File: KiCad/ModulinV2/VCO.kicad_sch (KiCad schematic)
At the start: 107 parts, among them IC13 AS3340D, IC14 AS3340D, IC15 TL074HIDR, IC16 TL074HIDR, IC17 TL072HIDR, Q1 MMBFJ201, Q2 MMBFJ201, SW1 SW_SPDT_MSM

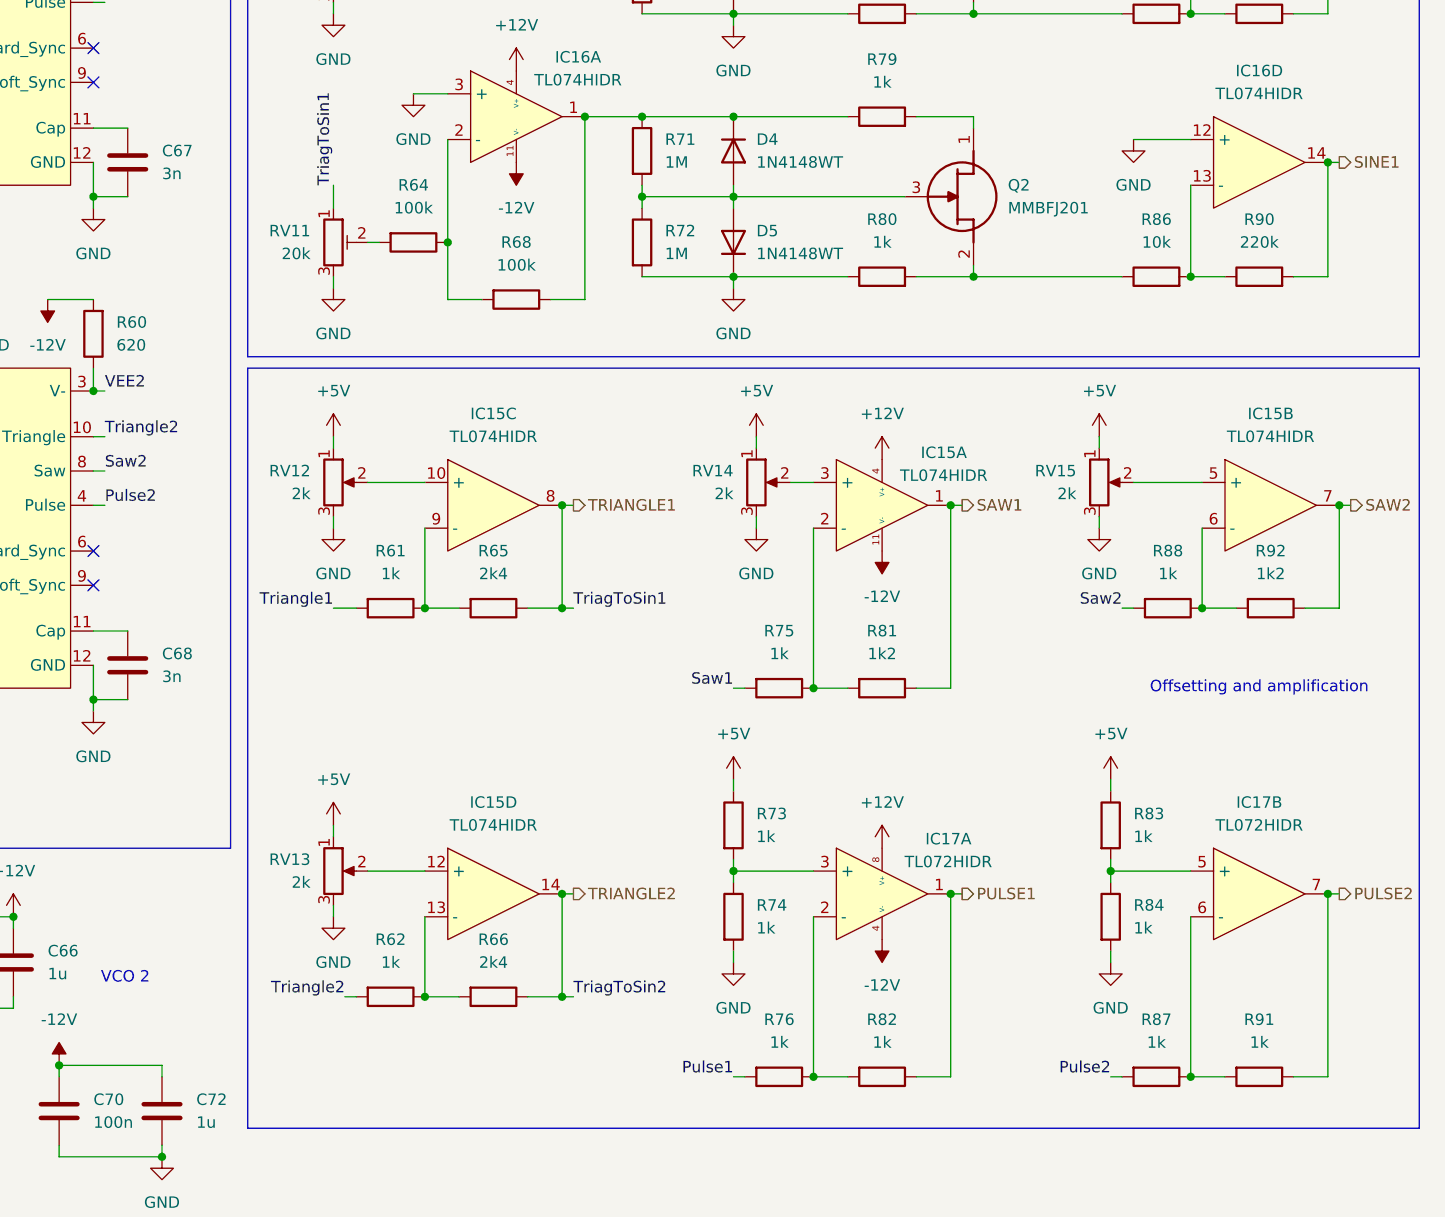
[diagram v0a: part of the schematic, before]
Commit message: Fixed schematic connections
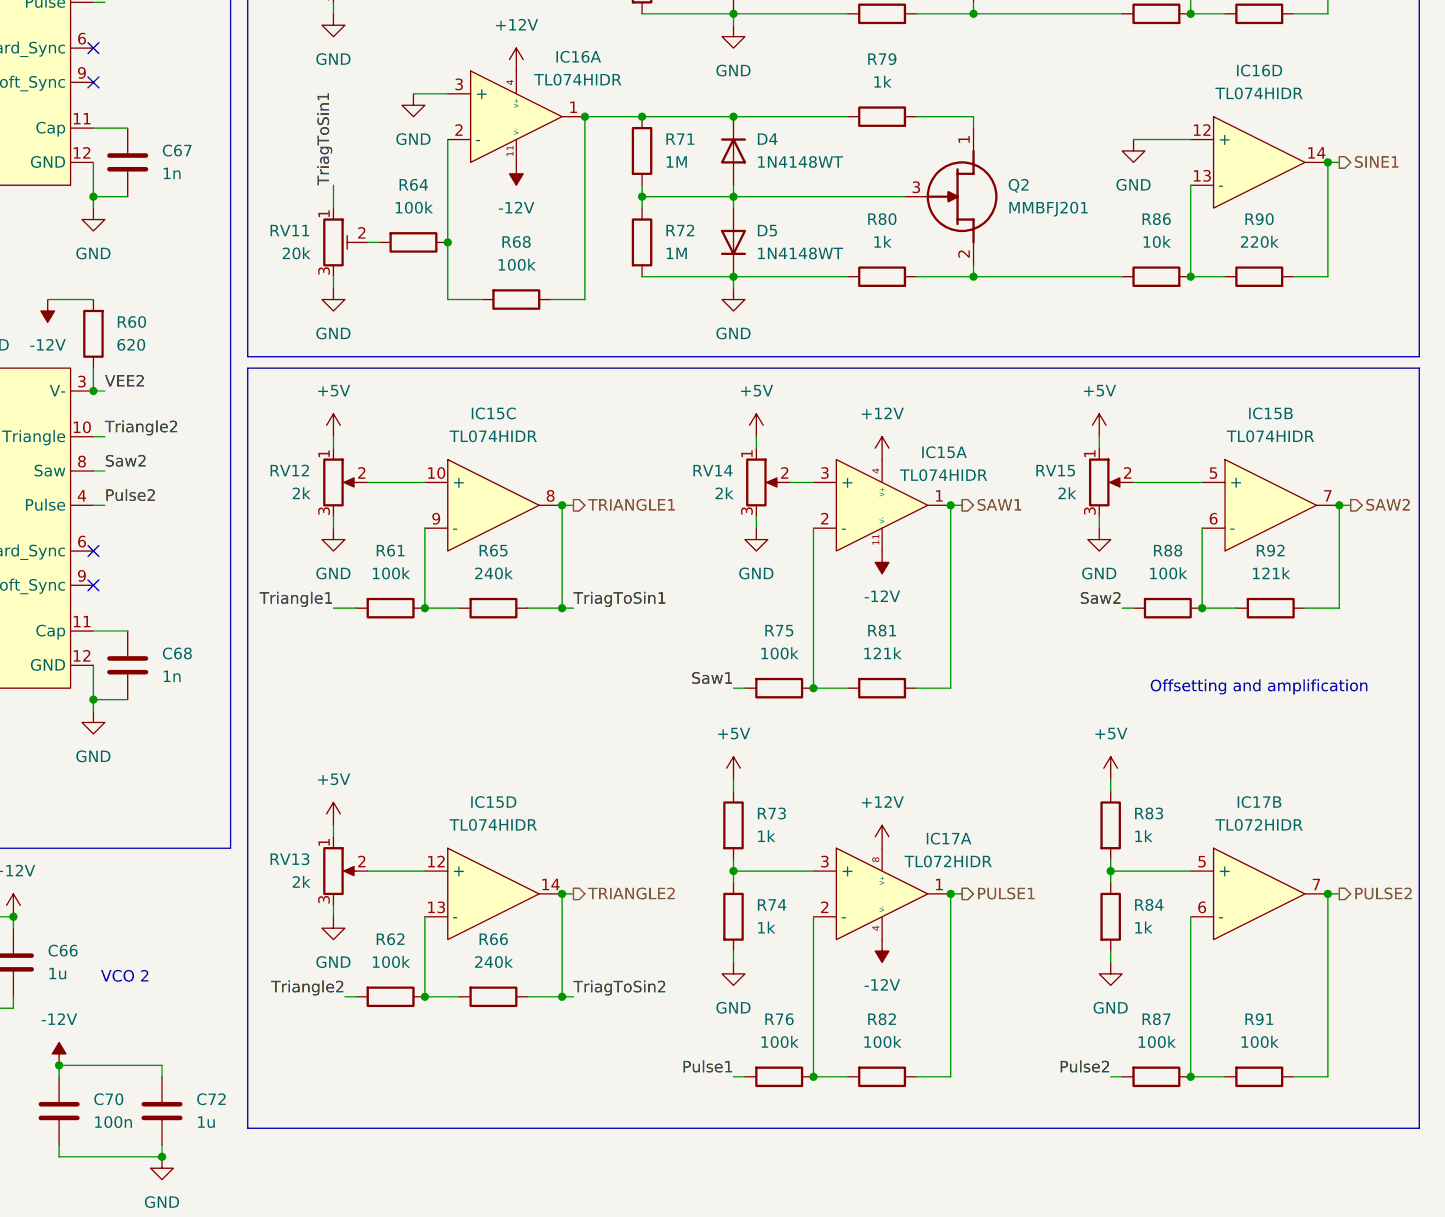
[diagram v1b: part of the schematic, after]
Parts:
- C67, C68: value 3n -> 1n
- R61, R62, R75, R76, R82, R87, R88, R91: value 1k -> 100k
- R65, R66: value 2k4 -> 240k
- R81, R92: value 1k2 -> 121k
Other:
- company: (none) -> TalTech
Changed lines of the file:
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@@
 	(title_block
 		(title "Voltage Controlled Oscillator")
-		(date "2025-07-13")
-		(rev "1.0")
+		(date "2026-04-29")
+		(rev "1.4")
+		(company "TalTech")
 		(comment 1 "Instructor: Kaiser Pärnamets")
-		(comment 2 "By: Rasmus Palk")
+		(comment 2 "Author: Rasmus Palk")
 	)
 	(rectangle
@@
 			)
 		)
-		(property "Value" "3n"
+		(property "Value" "1n"
 			(at 143.51 58.4199 0)
 			(effects
@@
 			)
 		)
-		(property "Value" "1k"
+		(property "Value" "100k"
 			(at 254 154.94 90)
 			(effects
@@
 			)
 		)
-		(property "Value" "1k"
+		(property "Value" "100k"
 			(at 255.27 102.87 90)
 			(effects
@@
 			)
 		)
-		(property "Value" "1k2"
+		(property "Value" "121k"
 			(at 266.7 102.87 90)
 			(effects
@@
 			)
 		)
-		(property "Value" "1k"
+		(property "Value" "100k"
 			(at 168.91 102.87 90)
 			(effects
@@
 			)
 		)
-		(property "Value" "1k"
+		(property "Value" "100k"
 			(at 212.09 154.94 90)
 			(effects
@@
 			)
 		)
-		(property "Value" "1k"
+		(property "Value" "100k"
 			(at 168.91 146.05 90)
 			(effects
@@
 			)
 		)
-		(property "Value" "1k"
+		(property "Value" "100k"
 			(at 223.52 154.94 90)
 			(effects
@@
 			)
 		)
-		(property "Value" "2k4"
+		(property "Value" "240k"
 			(at 180.34 146.05 90)
 			(effects
@@
 			)
 		)
-		(property "Value" "1k"
+		(property "Value" "100k"
 			(at 212.09 111.76 90)
 			(effects
@@
 			)
 		)
-		(property "Value" "1k2"
+		(property "Value" "121k"
 			(at 223.52 111.76 90)
 			(effects
@@
 			)
 		)
-		(property "Value" "2k4"
+		(property "Value" "240k"
 			(at 180.34 102.87 90)
 			(effects
@@
 			)
 		)
-		(property "Value" "3n"
+		(property "Value" "1n"
 			(at 143.51 114.2999 0)
 			(effects
@@
 			)
 		)
-		(property "Value" "1k"
+		(property "Value" "100k"
 			(at 265.43 154.94 90)
 			(effects
